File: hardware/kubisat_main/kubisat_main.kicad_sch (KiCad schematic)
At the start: 0 parts

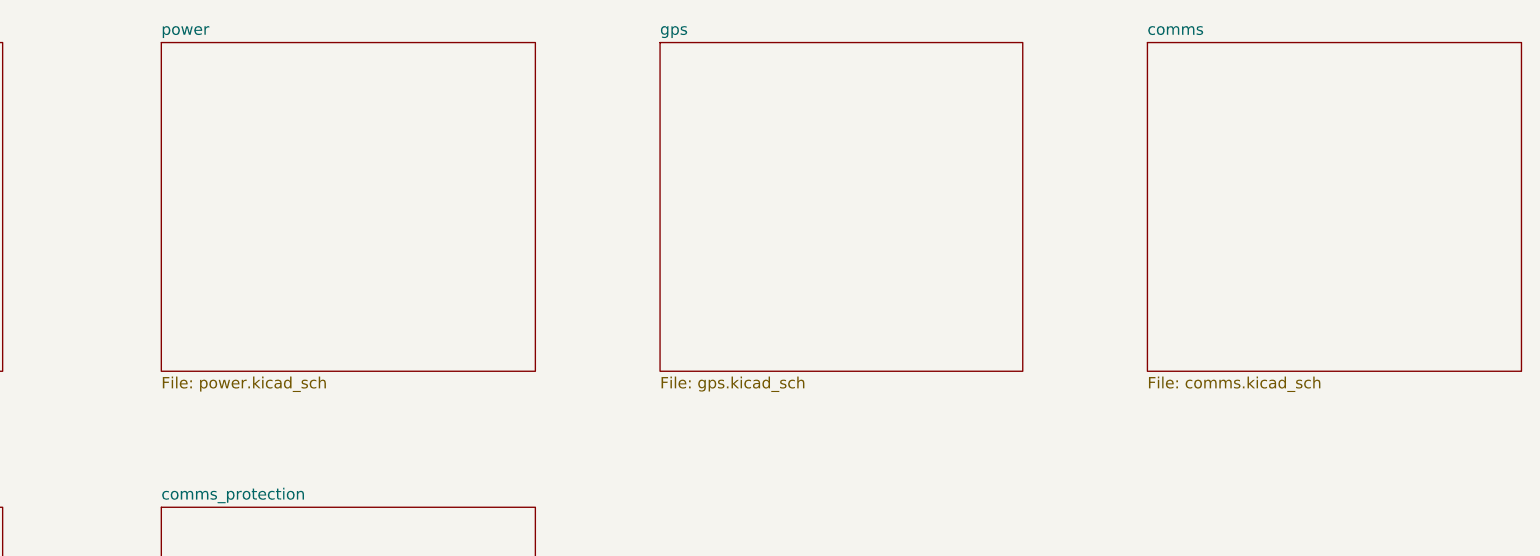
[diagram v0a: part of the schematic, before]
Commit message: added MCU based on arduino zeros ATSAMD21G18A
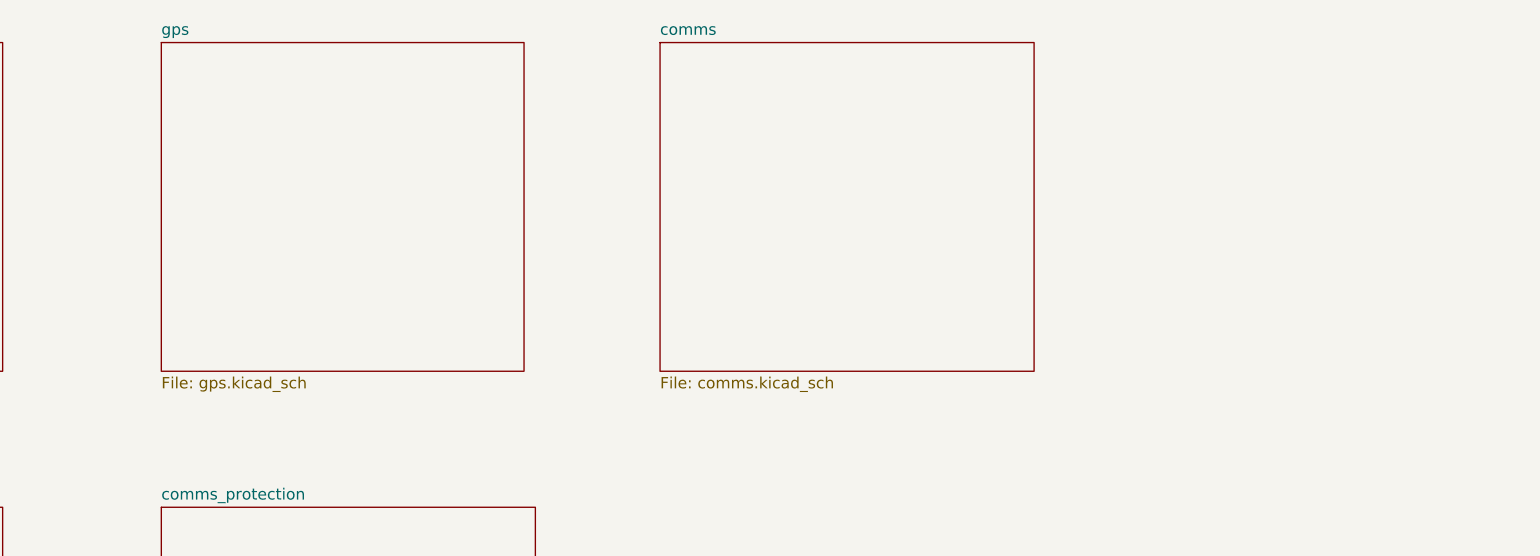
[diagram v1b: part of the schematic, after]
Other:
- removed sheet power
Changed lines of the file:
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@@
 	)
 	(sheet
-		(at 193.04 27.94)
+		(at 138.43 27.94)
 		(size 41.91 36.83)
 		(fields_autoplaced yes)
@@
 		)
 		(property "Sheetname" "comms"
-			(at 193.04 27.2284 0)
+			(at 138.43 27.2284 0)
 			(effects
 				(font
@@
 		)
 		(property "Sheetfile" "comms.kicad_sch"
-			(at 193.04 65.3546 0)
+			(at 138.43 65.3546 0)
 			(effects
 				(font
@@
 	)
 	(sheet
-		(at 138.43 27.94)
+		(at 82.55 27.94)
 		(size 40.64 36.83)
 		(fields_autoplaced yes)
@@
 		)
 		(property "Sheetname" "gps"
-			(at 138.43 27.2284 0)
+			(at 82.55 27.2284 0)
 			(effects
 				(font
@@
 		)
 		(property "Sheetfile" "gps.kicad_sch"
-			(at 138.43 65.3546 0)
+			(at 82.55 65.3546 0)
 			(effects
 				(font
@@
 				)
 			)
-		)
-	)
-	(sheet
-		(at 82.55 27.94)
-		(size 41.91 36.83)
-		(fields_autoplaced yes)
-		(stroke
-			(width 0.1524)
-			(type solid)
-		)
-		(fill
-			(color 0 0 0 0.0000)
-		)
-		(property "Sheetname" "power"
-			(at 82.55 27.2284 0)
-			(effects
-				(font
-					(size 1.27 1.27)
-				)
-				(justify left bottom)
-			)
-		)
-		(property "Sheetfile" "power.kicad_sch"
-			(at 82.55 65.3546 0)
-			(effects
-				(font
-					(size 1.27 1.27)
-				)
-				(justify left top)
-			)
-		)
-		(instances
-			(project "kubisat_main"
-				(path "/8e012760-7134-459b-b212-1cb69dd2e1ec"
-					(page "3")
-				)
-			)

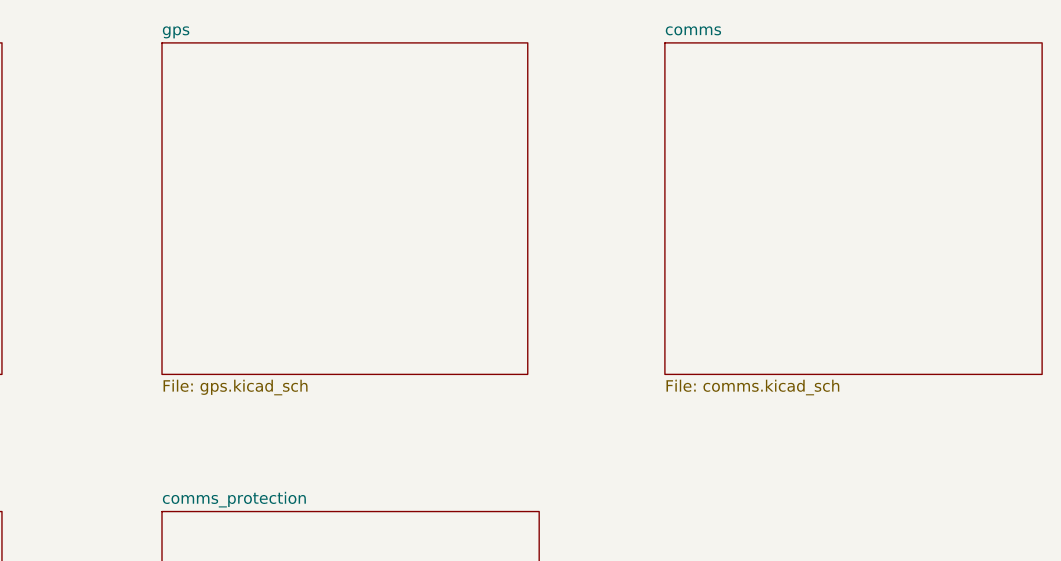
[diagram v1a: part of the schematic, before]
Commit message: added microsd footprint
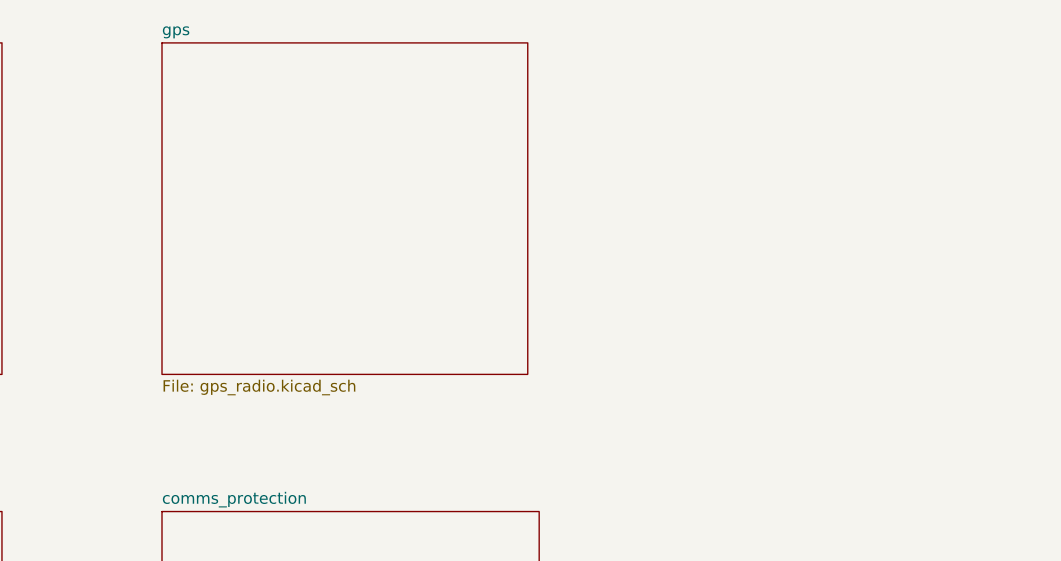
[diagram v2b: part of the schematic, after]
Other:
- removed sheet comms
- sheet gps: file gps.kicad_sch -> gps_radio.kicad_sch
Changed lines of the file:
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@@
-	)
-	(sheet
-		(at 138.43 27.94)
-		(size 41.91 36.83)
-		(fields_autoplaced yes)
-		(stroke
-			(width 0.1524)
-			(type solid)
-		)
-		(fill
-			(color 0 0 0 0.0000)
-		)
-		(property "Sheetname" "comms"
-			(at 138.43 27.2284 0)
-			(effects
-				(font
-					(size 1.27 1.27)
-				)
-				(justify left bottom)
-			)
-		)
-		(property "Sheetfile" "comms.kicad_sch"
-			(at 138.43 65.3546 0)
-			(effects
-				(font
-					(size 1.27 1.27)
-				)
-				(justify left top)
-			)
-		)
-		(instances
-			(project "kubisat_main"
-				(path "/8e012760-7134-459b-b212-1cb69dd2e1ec"
-					(page "5")
-				)
-			)
-		)
 	)
 	(sheet
@@
 			)
 		)
-		(property "Sheetfile" "gps.kicad_sch"
+		(property "Sheetfile" "gps_radio.kicad_sch"
 			(at 82.55 65.3546 0)
 			(effects

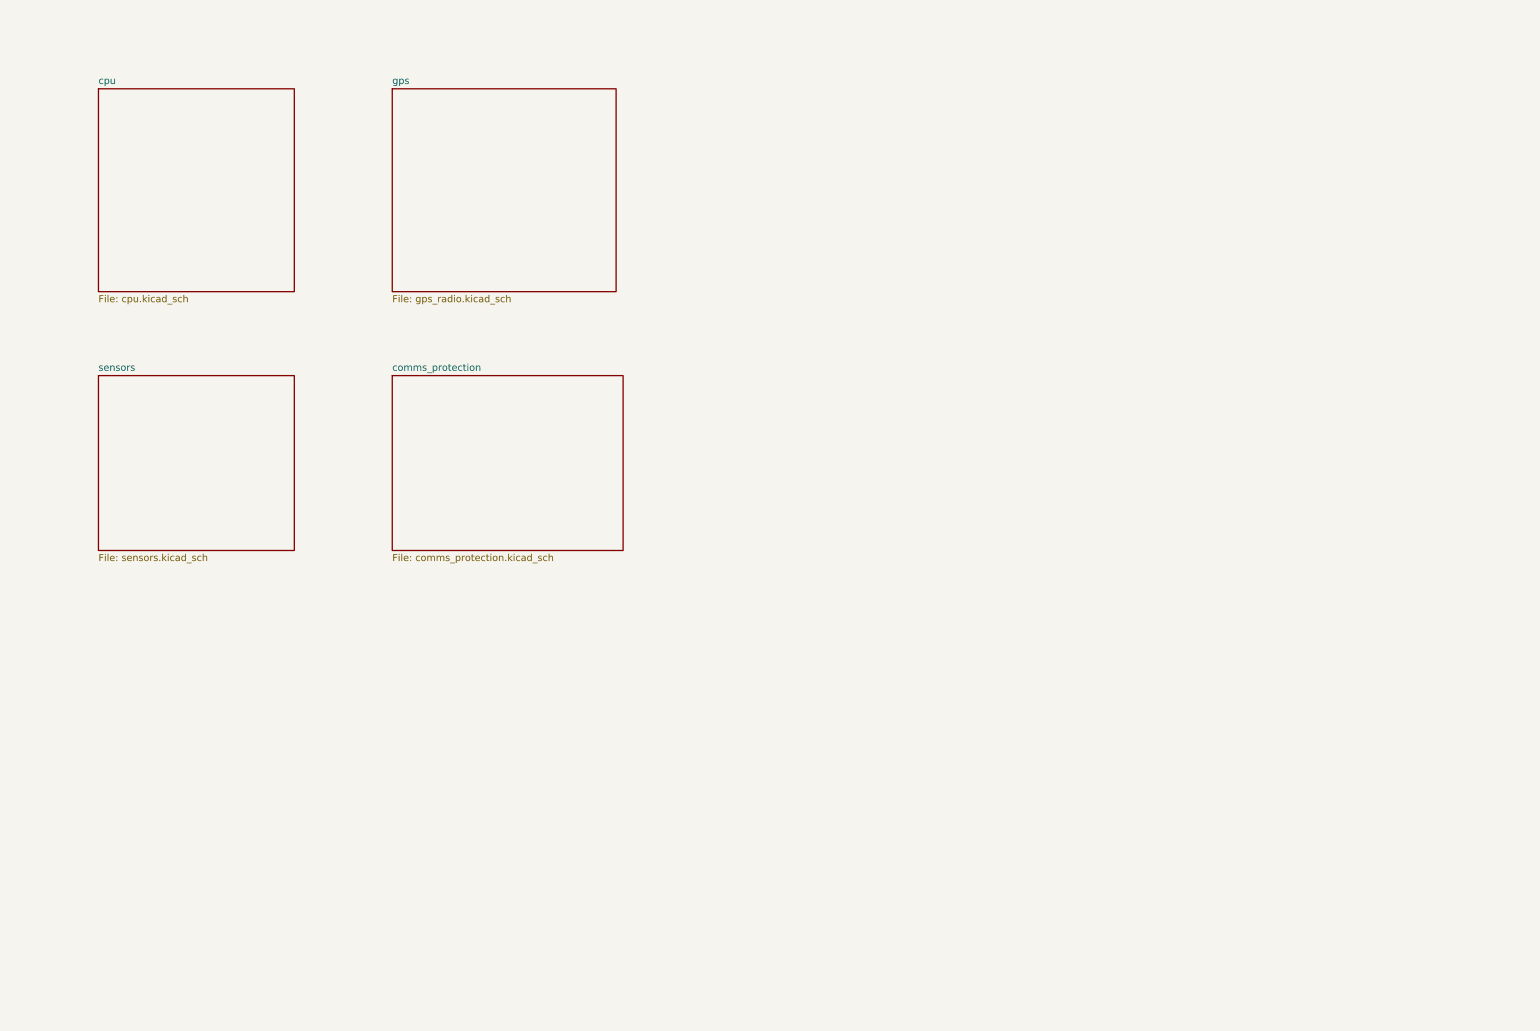
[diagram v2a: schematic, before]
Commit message: changed strucutre, split main into 2 sseparate boards
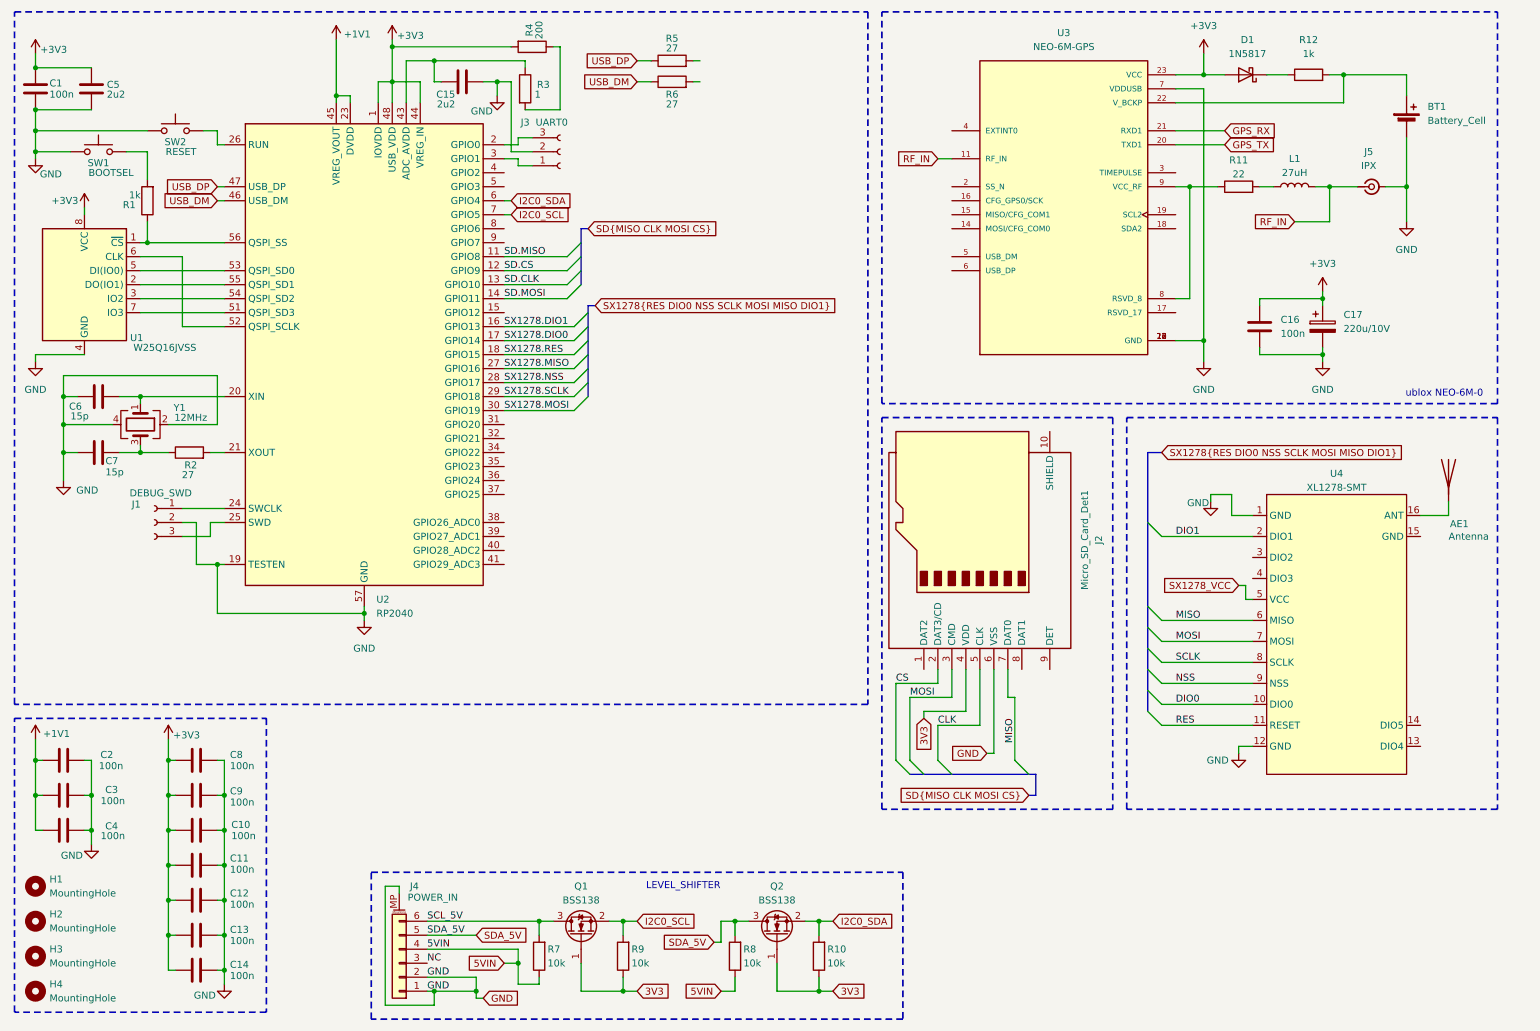
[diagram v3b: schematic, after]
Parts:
- added AE1: Antenna, symbol Device:Antenna
- added BT1: Battery_Cell, Battery:BatteryHolder_Seiko_MS621F, symbol Device:Battery_Cell
- added C1, C10, C11, C12, C13, C14, C16, C2, C3, C4, C8, C9: 100n, Capacitor_SMD:C_0805_2012Metric, symbol Device:C
- added C15, C5: 2u2, Capacitor_SMD:C_0805_2012Metric, symbol Device:C
- added C17: 220u/10V, Capacitor_Tantalum_SMD:CP_EIA-6032-15_Kemet-U, symbol Device:C_Polarized
- added C6, C7: 15p, Capacitor_SMD:C_0805_2012Metric, symbol Device:C
- added D1: 1N5817, Diode_SMD:D_SOD-123, symbol Device:D_Schottky
- added H1, H2, H3, H4: MountingHole, MountingHole:MountingHole_3.2mm_M3_DIN965, symbol Mechanical:MountingHole
- added J1: DEBUG_SWD, Connector_PinHeader_1.00mm:PinHeader_1x03_P1.00mm_Vertical, symbol Connector:Conn_01x03_Socket
- added J2: Micro_SD_Card_Det1, Connector_Card:MR01A-01211, symbol Connector:Micro_SD_Card_Det1
- added J3: UART0, Connector_PinHeader_1.00mm:PinHeader_1x03_P1.00mm_Vertical, symbol Connector:Conn_01x03_Socket
- added J4: POWER_IN, Connector_JST:JST_PH_S6B-PH-SM4-TB_1x06-1MP_P2.00mm_Horizontal, symbol Connector_Generic_MountingPin:Conn_01x06_MountingPin
- added J5: IPX, Connector_Coaxial:U.FL_Hirose_U.FL-R-SMT-1_Vertical, symbol Connector:Conn_Coaxial_Small
- added L1: 27uH, Inductor_SMD:L_0805_2012Metric, symbol Device:L
- added Q1, Q2: BSS138, Package_TO_SOT_SMD:SOT-23, symbol Transistor_FET:BSS138
- added R1: 1k, symbol Device:R
- added R10, R7, R8, R9: 10k, symbol Device:R
- added R11: 22, Resistor_SMD:R_0805_2012Metric, symbol Device:R
- added R12: 1k, Resistor_SMD:R_0805_2012Metric, symbol Device:R
- added R2, R5, R6: 27, symbol Device:R
- added R3: 1, symbol Device:R
- added R4: 200, symbol Device:R
- added SW1: BOOTSEL, Button_Switch_SMD:SW_MEC_5GSH9, symbol Switch:SW_Push
- added SW2: RESET, Button_Switch_SMD:SW_MEC_5GSH9, symbol Switch:SW_Push
- added U1: W25Q16JVSS, Package_SO:SOIC-8_5.23x5.23mm_P1.27mm, symbol Memory_Flash:W25Q16JVSS
- added U2: RP2040, Package_DFN_QFN:QFN-56-1EP_7x7mm_P0.4mm_EP3.2x3.2mm, symbol MCU_RaspberryPi:RP2040
- added U3: NEO-6M-GPS, RF_GPS:ublox_NEO, symbol RF_GPS:NEO-6M-GPS
- added U4: XL1278-SMT, RF:XL1278-SMT, symbol RF:XL1278-SMT
- added Y1: 12MHz, Crystal:Crystal_SMD_3225-4Pin_3.2x2.5mm, symbol Device:Crystal_GND24
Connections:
- new net: R3.2, R4.1
- new net: C7.2, R2.1, Y1.3
- new net: R2.2, U2.21 (XOUT)
- new net: AE1.1 (A), U4.16 (ANT)
- new net: D1.1 (K), R12.1
- new net: BT1.1 (+), R12.2, U3.22 (V_BCKP)
- new net: SW2.2, U2.26 (RUN)
- new net: R1.1, U1.1 (~{CS}), U2.56 (QSPI_SS)
- new net: U1.2 (DO(IO1)), U2.55 (QSPI_SD1)
- new net: U1.3 (IO2), U2.54 (QSPI_SD2)
- new net: U1.5 (DI(IO0)), U2.53 (QSPI_SD0)
- new net: U1.6 (CLK), U2.52 (QSPI_SCLK)
- new net: U1.7 (IO3), U2.51 (QSPI_SD3)
- new net: J1.1 (Pin_1), U2.24 (SWCLK)
- new net: J1.3 (Pin_3), U2.25 (SWD)
- new net: C15.2, R3.1, U2.43 (ADC_AVDD)
- new net: J3.3 (Pin_3), U2.2 (GPIO0)
- new net: C6.2, U2.20 (XIN), Y1.1
- new net: J3.1 (Pin_1), U2.3 (GPIO1)
- new net: R1.2, SW1.2
- new net: R11.1, U3.8 (RSVD_8), U3.9 (VCC_RF)
- new net: L1.1, R11.2
- new net +1V1: C2.1, C3.2, C4.2, U2.23 (DVDD), U2.45 (VREG_VOUT), U2.50 (DVDD)
- new net +3V3: C1.2, C10.1, C11.1, C12.1, C13.1, C14.1, C16.1, C17.1, C5.2, C8.1, C9.1, D1.2 (A), R4.2, U1.8 (VCC), U2.1 (IOVDD), U2.10 (IOVDD), U2.22 (IOVDD), U2.33 (IOVDD), U2.42 (IOVDD), U2.44 (VREG_IN), U2.48 (USB_VDD), U2.49 (IOVDD), U3.23 (VCC)
- new net 3V3: J2.4 (VDD), Q1.1 (G), Q2.1 (G), R10.1, R9.1
- new net 5VIN: J4.4 (Pin_4), R7.1, R8.1
- new net CLK: J2.5 (CLK)
- new net CS: J2.2 (DAT3/CD)
- new net DIO0: U4.10 (DIO0)
- new net DIO1: U4.2 (DIO1)
- new net GND: BT1.2 (-), C1.1, C10.2, C11.2, C12.2, C13.2, C14.2, C15.1, C16.2, C17.2, C2.2, C3.1, C4.1, C5.1, C6.1, C7.1, C8.2, C9.2, J1.2 (Pin_2), J2.6 (VSS), J3.2 (Pin_2), J4.1 (Pin_1), J4.2 (Pin_2), J4.MP (MountPin), J5.2 (Ext), SW1.1, SW2.1, U1.4 (GND), U2.19 (TESTEN), U2.57 (GND), U3.10 (GND), U3.12 (GND), U3.13 (GND), U3.24 (GND), U3.7 (VDDUSB), U4.1 (GND), U4.12 (GND), Y1.2, Y1.4
- new net GPS_RX: U3.21 (RXD1)
- new net GPS_TX: U3.20 (TXD1)
- new net I2C0_SCL: Q1.2 (S), R9.2, U2.7 (GPIO5)
- new net I2C0_SDA: Q2.2 (S), R10.2, U2.6 (GPIO4)
- new net MISO: J2.7 (DAT0), U4.6 (MISO)
- new net MOSI: J2.3 (CMD), U4.7 (MOSI)
- new net NC: J4.3 (Pin_3)
- new net NSS: U4.9 (NSS)
- new net RES: U4.11 (RESET)
- new net RF_IN: J5.1 (In), L1.2, U3.11 (RF_IN)
- new net SCLK: U4.8 (SCLK)
- new net SCL_5V: J4.6 (Pin_6), Q1.3 (D), R7.2
- new net SD.CLK: U2.13 (GPIO10)
- new net SD.CS: U2.12 (GPIO9)
- new net SD.MISO: U2.11 (GPIO8)
- new net SD.MOSI: U2.14 (GPIO11)
- new net SDA_5V: J4.5 (Pin_5), Q2.3 (D), R8.2
- new net SX1278.DIO0: U2.17 (GPIO14)
- new net SX1278.DIO1: U2.16 (GPIO13)
- new net SX1278.MISO: U2.27 (GPIO16)
- new net SX1278.MOSI: U2.30 (GPIO19)
- new net SX1278.NSS: U2.28 (GPIO17)
- new net SX1278.RES: U2.18 (GPIO15)
- new net SX1278.SCLK: U2.29 (GPIO18)
- new net SX1278_VCC: U4.5 (VCC)
- new net USB_DM: R6.1, U2.46 (USB_DM)
- new net USB_DP: R5.1, U2.47 (USB_DP)
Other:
- removed sheet comms_protection
- removed sheet cpu
- removed sheet gps
- removed sheet sensors
- note added: "LEVEL_SHIFTER"
- note added: "ublox NEO-6M-0"
